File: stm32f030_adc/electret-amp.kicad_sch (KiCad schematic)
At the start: 13 parts, among them Q1 BC337

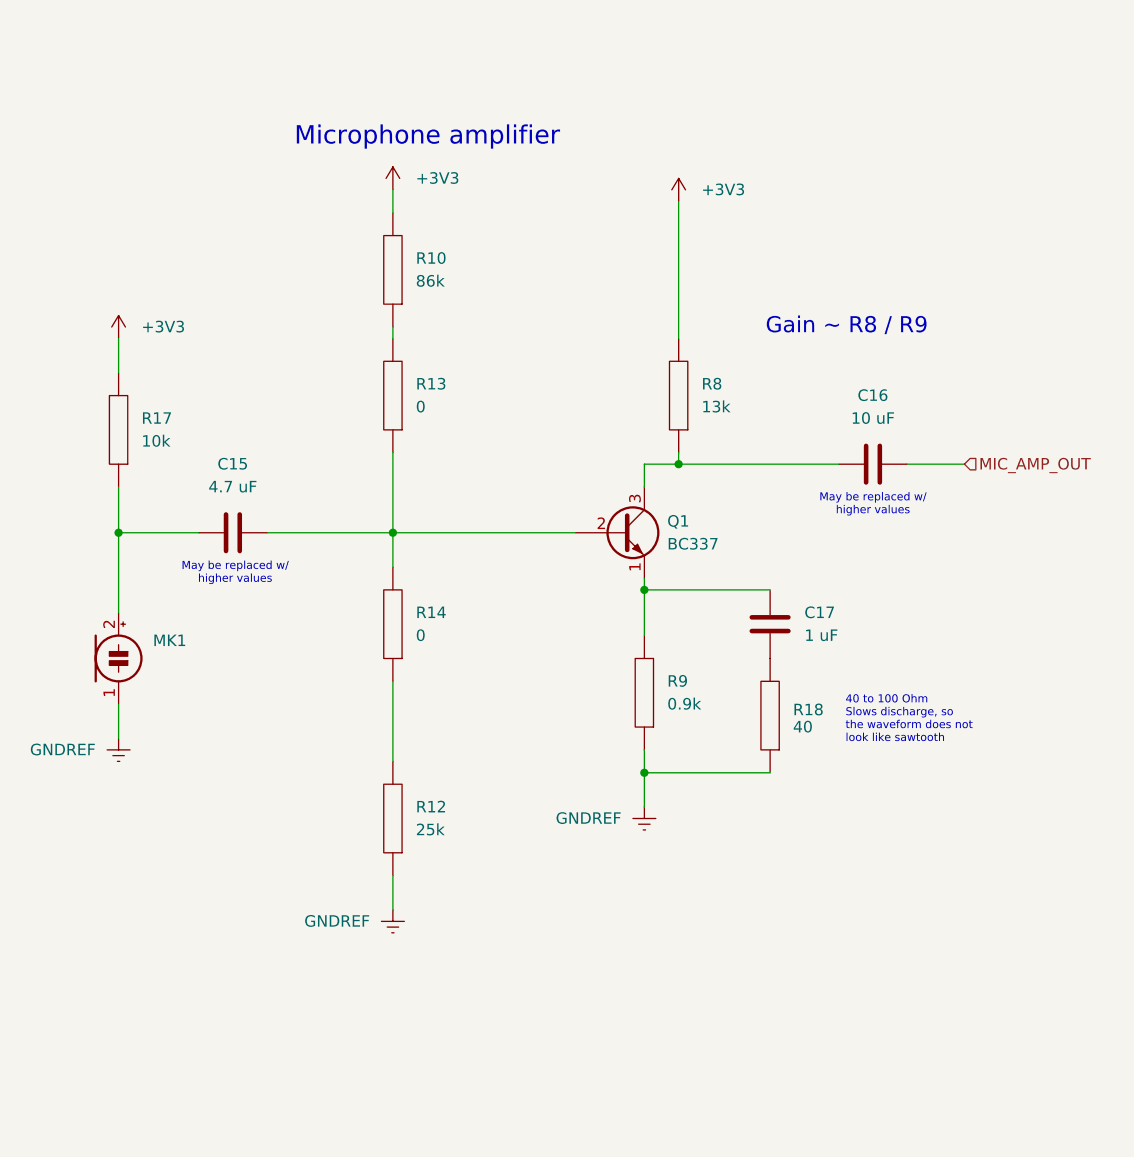
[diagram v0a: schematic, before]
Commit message: Extensibility: more jumpers, intermediate result, the layout is not complete
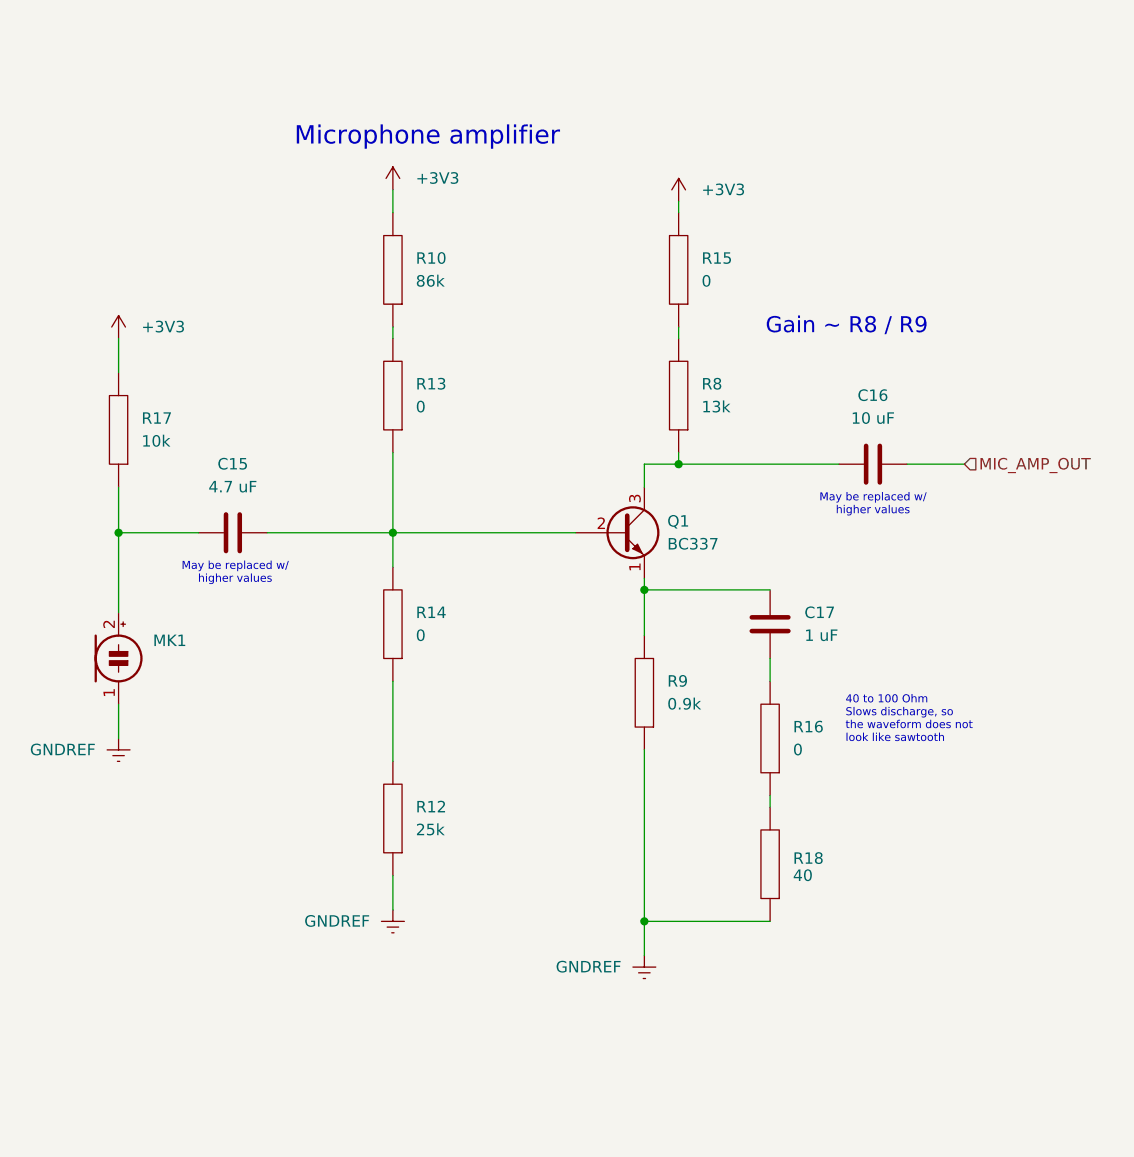
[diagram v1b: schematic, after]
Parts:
- added R15, R16: 0, Resistor_THT:R_Axial_DIN0207_L6.3mm_D2.5mm_P10.16mm_Horizontal, symbol pspice:R
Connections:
- net +3V3: now also R15.2; no longer R8.2
- net at R18.2: now also R16.1; no longer C17.1
- new net: R15.1, R8.2
- new net: C17.1, R16.2
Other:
- moved on the sheet: R18
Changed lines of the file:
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@@
-	)
-	(junction
-		(at 153.67 127)
-		(diameter 0)
-		(color 0 0 0 0)
 	)
 	(junction
@@
 		(color 0 0 0 0)
 	)
+	(junction
+		(at 153.67 143.51)
+		(diameter 0)
+		(color 0 0 0 0)
+	)
 	(wire
 		(pts
@@
 	(wire
 		(pts
+			(xy 157.48 77.47) (xy 157.48 78.74)
+		)
+		(stroke
+			(width 0)
+			(type default)
+		)
+	)
+	(wire
+		(pts
 			(xy 125.73 116.84) (xy 125.73 125.73)
 		)
@@
 	(wire
 		(pts
+			(xy 167.64 116.84) (xy 167.64 114.3)
+		)
+		(stroke
+			(width 0)
+			(type default)
+		)
+	)
+	(wire
+		(pts
 			(xy 153.67 92.71) (xy 153.67 95.25)
 		)
@@
 	(wire
 		(pts
-			(xy 153.67 127) (xy 153.67 130.81)
+			(xy 153.67 124.46) (xy 153.67 143.51)
 		)
 		(stroke
@@
 	(wire
 		(pts
+			(xy 153.67 143.51) (xy 153.67 147.32)
+		)
+		(stroke
+			(width 0)
+			(type default)
+		)
+	)
+	(wire
+		(pts
+			(xy 167.64 130.81) (xy 167.64 129.54)
+		)
+		(stroke
+			(width 0)
+			(type default)
+		)
+	)
+	(wire
+		(pts
 			(xy 182.88 92.71) (xy 189.23 92.71)
 		)
@@
 	(wire
 		(pts
-			(xy 153.67 127) (xy 167.64 127)
-		)
-		(stroke
-			(width 0)
-			(type default)
-		)
-	)
-	(wire
-		(pts
-			(xy 157.48 63.5) (xy 157.48 78.74)
+			(xy 153.67 143.51) (xy 167.64 143.51)
+		)
+		(stroke
+			(width 0)
+			(type default)
+		)
+	)
+	(wire
+		(pts
+			(xy 157.48 63.5) (xy 157.48 64.77)
 		)
 		(stroke
@@
 		(pts
 			(xy 125.73 138.43) (xy 125.73 142.24)
-		)
-		(stroke
-			(width 0)
-			(type default)
-		)
-	)
-	(wire
-		(pts
-			(xy 153.67 124.46) (xy 153.67 127)
 		)
 		(stroke
@@
 	(symbol
 		(lib_id "power:GNDREF")
-		(at 153.67 130.81 0)
+		(at 153.67 147.32 0)
 		(mirror y)
 		(unit 1)
@@
 		(fields_autoplaced yes)
 		(property "Reference" "#PWR013"
-			(at 153.67 137.16 0)
+			(at 153.67 153.67 0)
 			(effects
 				(font
@@
 		)
 		(property "Value" "GNDREF"
-			(at 151.13 132.0799 0)
+			(at 151.13 148.5899 0)
 			(effects
 				(font
@@
 		)
 		(property "Footprint" ""
-			(at 153.67 130.81 0)
+			(at 153.67 147.32 0)
 			(effects
 				(font
@@
 		)
 		(property "Datasheet" ""
-			(at 153.67 130.81 0)
+			(at 153.67 147.32 0)
 			(effects
 				(font
@@
 		)
 		(property "Description" ""
-			(at 153.67 130.81 0)
+			(at 153.67 147.32 0)
 			(effects
 				(font
@@
 				(path "/85629656-c73b-4e1f-b8e8-4366f4b01266/f519304b-9da7-41e0-88ca-532cf10653e0"
 					(reference "#PWR013")
+					(unit 1)
+				)
+			)
+		)
+	)
+	(symbol
+		(lib_id "pspice:R")
+		(at 167.64 123.19 180)
+		(unit 1)
+		(exclude_from_sim no)
+		(in_bom yes)
+		(on_board yes)
+		(dnp no)
+		(fields_autoplaced yes)
+		(property "Reference" "R16"
+			(at 170.18 121.9199 0)
+			(effects
+				(font
+					(size 1.27 1.27)
+				)
+				(justify right)
+			)
+		)
+		(property "Value" "0"
+			(at 170.18 124.4599 0)
+			(effects
+				(font
+					(size 1.27 1.27)
+				)
+				(justify right)
+			)
+		)
+		(property "Footprint" "Resistor_THT:R_Axial_DIN0207_L6.3mm_D2.5mm_P10.16mm_Horizontal"
+			(at 167.64 123.19 0)
+			(effects
+				(font
+					(size 1.27 1.27)
+				)
+				(hide yes)
+			)
+		)
+		(property "Datasheet" "~"
+			(at 167.64 123.19 0)
+			(effects
+				(font
+					(size 1.27 1.27)
+				)
+				(hide yes)
+			)
+		)
+		(property "Description" ""
+			(at 167.64 123.19 0)
+			(effects
+				(font
+					(size 1.27 1.27)
+				)
+				(hide yes)
+			)
+		)
+		(pin "1"
+		)
+		(pin "2"
+		)
+		(instances
+			(project "stm32f030_adc"
+				(path "/85629656-c73b-4e1f-b8e8-4366f4b01266/f519304b-9da7-41e0-88ca-532cf10653e0"
+					(reference "R16")
 					(unit 1)
 				)
@@
 	(symbol
 		(lib_id "pspice:R")
-		(at 167.64 120.65 180)
+		(at 167.64 137.16 180)
 		(unit 1)
 		(exclude_from_sim no)
@@
 		(dnp no)
 		(property "Reference" "R18"
-			(at 170.18 120.0149 0)
+			(at 170.18 136.5249 0)
 			(effects
 				(font
@@
 		)
 		(property "Value" "40"
-			(at 170.18 121.92 0)
+			(at 170.18 138.43 0)
 			(effects
 				(font
@@
 		)
 		(property "Footprint" "Resistor_THT:R_Axial_DIN0207_L6.3mm_D2.5mm_P10.16mm_Horizontal"
-			(at 167.64 120.65 0)
+			(at 167.64 137.16 0)
 			(effects
 				(font
@@
 		)
 		(property "Datasheet" "~"
-			(at 167.64 120.65 0)
+			(at 167.64 137.16 0)
 			(effects
 				(font
@@
 		)
 		(property "Description" ""
-			(at 167.64 120.65 0)
+			(at 167.64 137.16 0)
 			(effects
 				(font
@@
 					(unit 1)
 				)
+			)
+		)
+	)
+	(symbol
+		(lib_id "pspice:R")
+		(at 157.48 71.12 180)
+		(unit 1)
+		(exclude_from_sim no)
+		(in_bom yes)
+		(on_board yes)
+		(dnp no)
+		(fields_autoplaced yes)
+		(property "Reference" "R15"
+			(at 160.02 69.8499 0)
+			(effects
+				(font
+					(size 1.27 1.27)
+				)
+				(justify right)
+			)
+		)
+		(property "Value" "0"
+			(at 160.02 72.3899 0)
+			(effects
+				(font
+					(size 1.27 1.27)
+				)
+				(justify right)
+			)
+		)
+		(property "Footprint" "Resistor_THT:R_Axial_DIN0207_L6.3mm_D2.5mm_P10.16mm_Horizontal"
+			(at 157.48 71.12 0)
+			(effects
+				(font
+					(size 1.27 1.27)
+				)
+				(hide yes)
+			)
+		)
+		(property "Datasheet" "~"
+			(at 157.48 71.12 0)
+			(effects
+				(font
+					(size 1.27 1.27)
+				)
+				(hide yes)
+			)
+		)
+		(property "Description" ""
+			(at 157.48 71.12 0)
+			(effects
+				(font
+					(size 1.27 1.27)
+				)
+				(hide yes)
+			)
+		)
+		(pin "1"
+		)
+		(pin "2"
+		)
+		(instances
+			(project "stm32f030_adc"
+				(path "/85629656-c73b-4e1f-b8e8-4366f4b01266/f519304b-9da7-41e0-88ca-532cf10653e0"
+					(reference "R15")
+					(unit 1)
+				)

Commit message: Narrowed
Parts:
- added R19, R20, R21, R22: 0, Resistor_THT:R_Axial_DIN0207_L6.3mm_D2.5mm_P10.16mm_Horizontal, symbol pspice:R
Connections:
- net +3V3: now also R21.2, R22.2; no longer R10.2, R15.2
- net at R16.1: now also R19.2; no longer R18.2
- net at C15.2, Q1.2 (B), R13.1: now also R20.2; no longer R14.2
- new net: R18.2, R19.1
- new net: R14.2, R20.1
- new net: R10.2, R21.1
- new net: R15.2, R22.1
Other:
- moved on the sheet: R12, R14, R18
